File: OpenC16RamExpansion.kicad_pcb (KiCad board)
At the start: 2 copper layers, 51.1 x 45 mm, 6 parts, among them J1 C16-Exp-Port, U1 74LS257, U2 74LS257, U3 4464, U4 4464

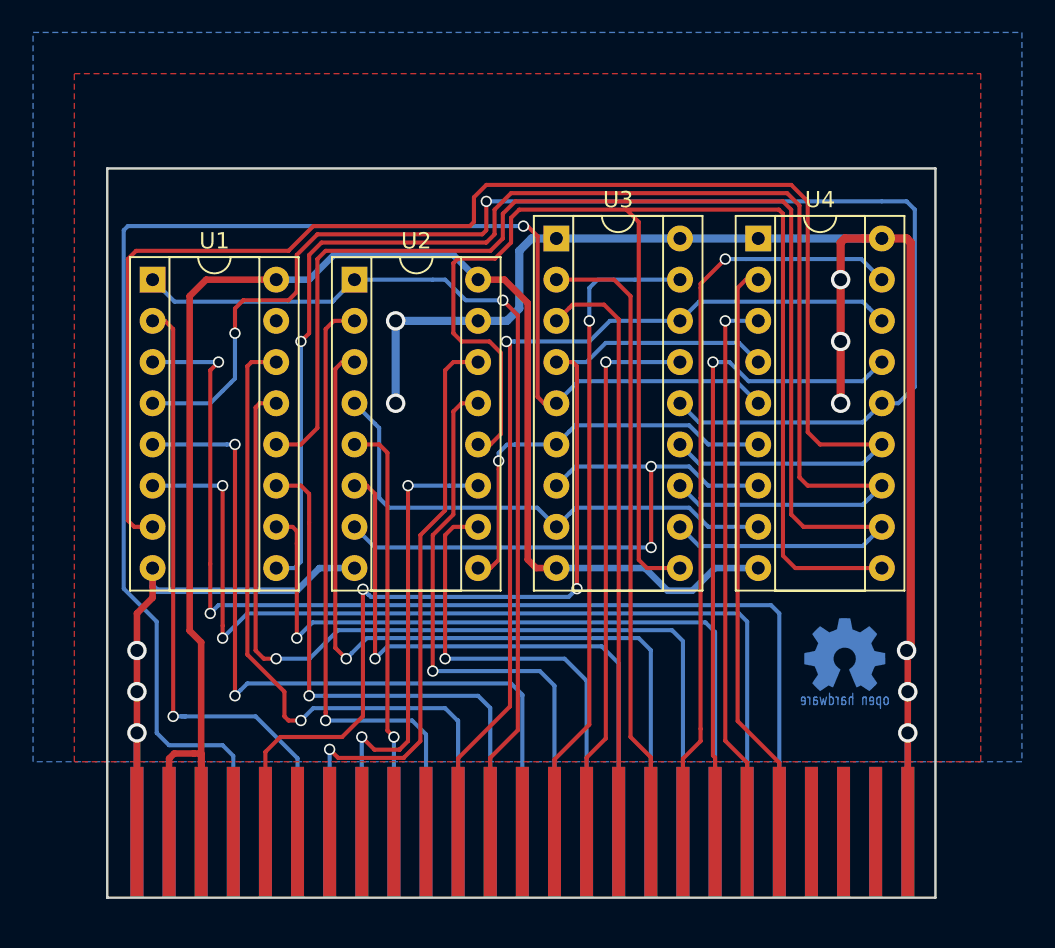
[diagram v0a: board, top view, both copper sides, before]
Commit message: Switch to new connector and improve back ground plane
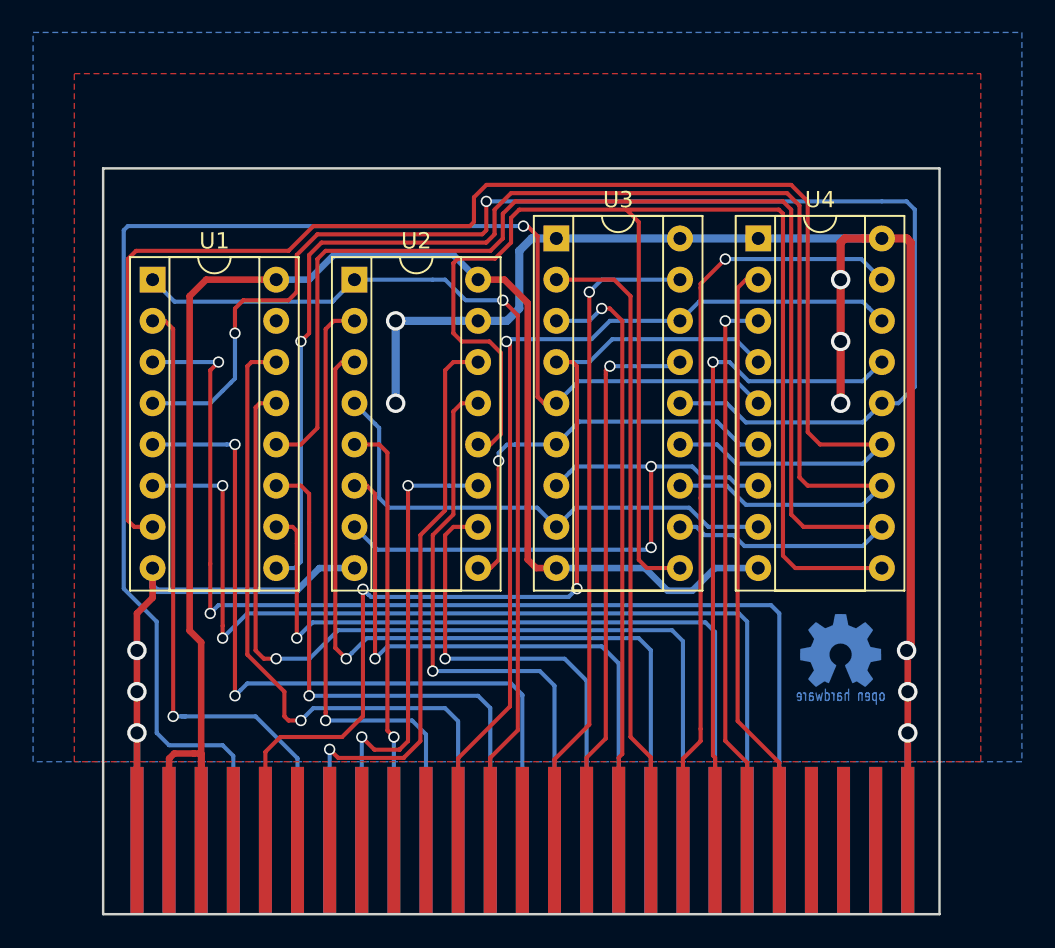
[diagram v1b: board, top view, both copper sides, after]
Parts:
- moved J1 1.00 mm to (149.5, 143.2)
- moved G*** 0.36 mm to (169.2, 127.0)
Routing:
- net /d5: track 36.2 -> 36.3 mm, vias 0 -> 1
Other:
- board size 51.1 x 45 mm -> 51.6 x 46 mm
- board text added: "V1.1"
- board text removed: "V1.0"

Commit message: Make connector lower again and smooth orners
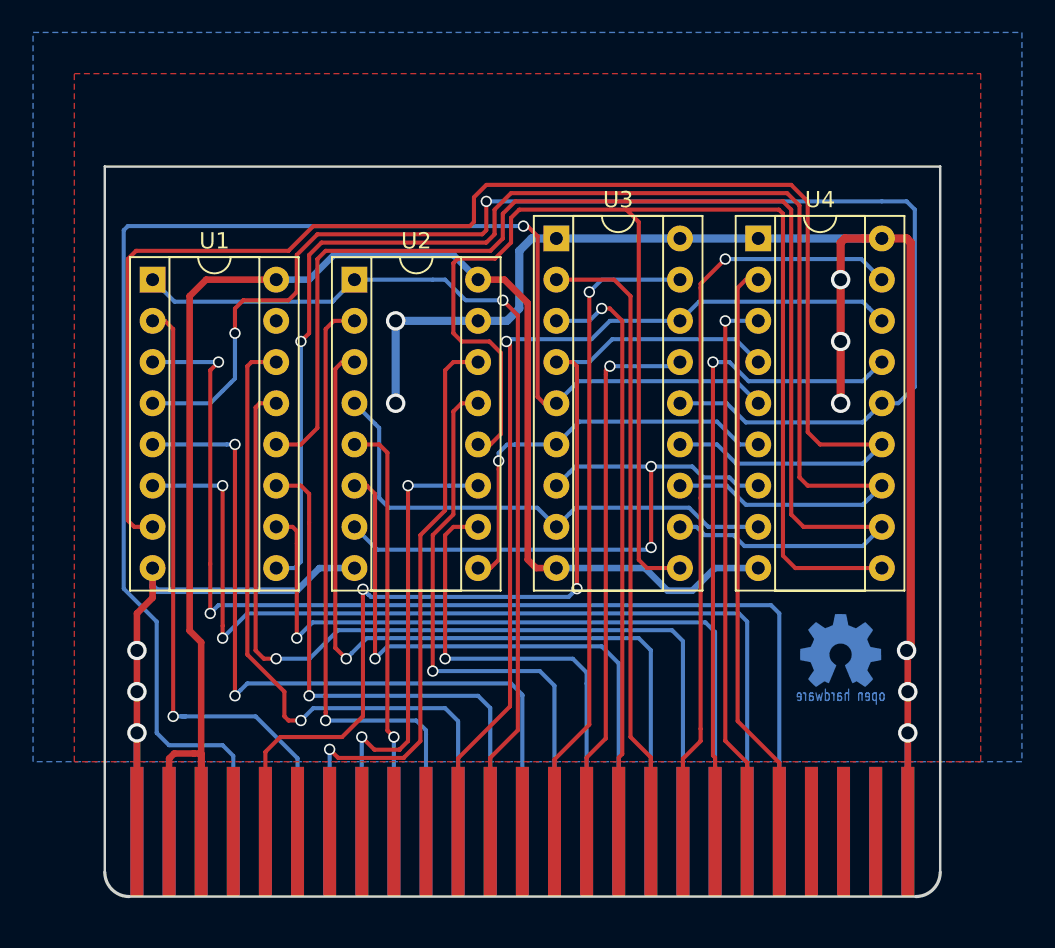
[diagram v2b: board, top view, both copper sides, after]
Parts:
- moved J1 5.00 mm to (149.5, 138.2)
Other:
- board size 51.6 x 46 mm -> 51.5 x 45 mm
- board text added: "github.com/SukkoPera/OpenC16RamExpansion"
- board text removed: "https://github.com/SukkoPera/OpenC16RamExpansion"

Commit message: Add decoupling caps
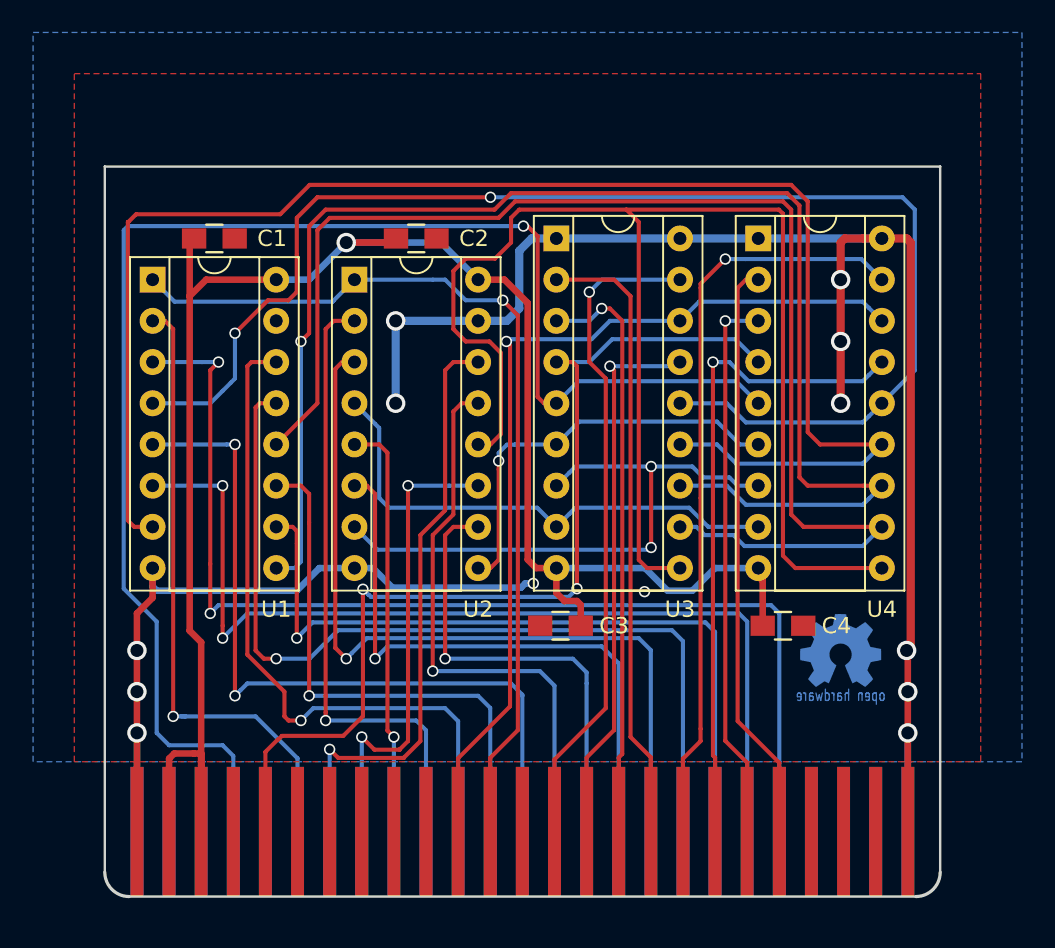
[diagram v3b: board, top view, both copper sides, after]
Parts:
- added C1: C, Capacitors_SMD:C_0805_HandSoldering, F.Cu at (130.6, 101.6)
- added C2: C, Capacitors_SMD:C_0805_HandSoldering, F.Cu at (143.0, 101.6)
- added C3: C, Capacitors_SMD:C_0805_HandSoldering, F.Cu at (151.9, 125.5)
- added C4: C, Capacitors_SMD:C_0805_HandSoldering, F.Cu at (165.6, 125.5)
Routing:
- net VCC: track 95.2 -> 112.1 mm, vias 0 -> 1
- net GND: track 133.5 -> 145.1 mm, vias 11 -> 12
- net /a0: track 84.1 -> 83.1 mm
- net /d7: track 40.1 -> 40.9 mm
- net /a3: track 83.3 -> 82.5 mm
- net (no net): vias 0 -> 1

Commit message: Space edge connector pins 2.0mm apart, improve ground plane and some other tweaks
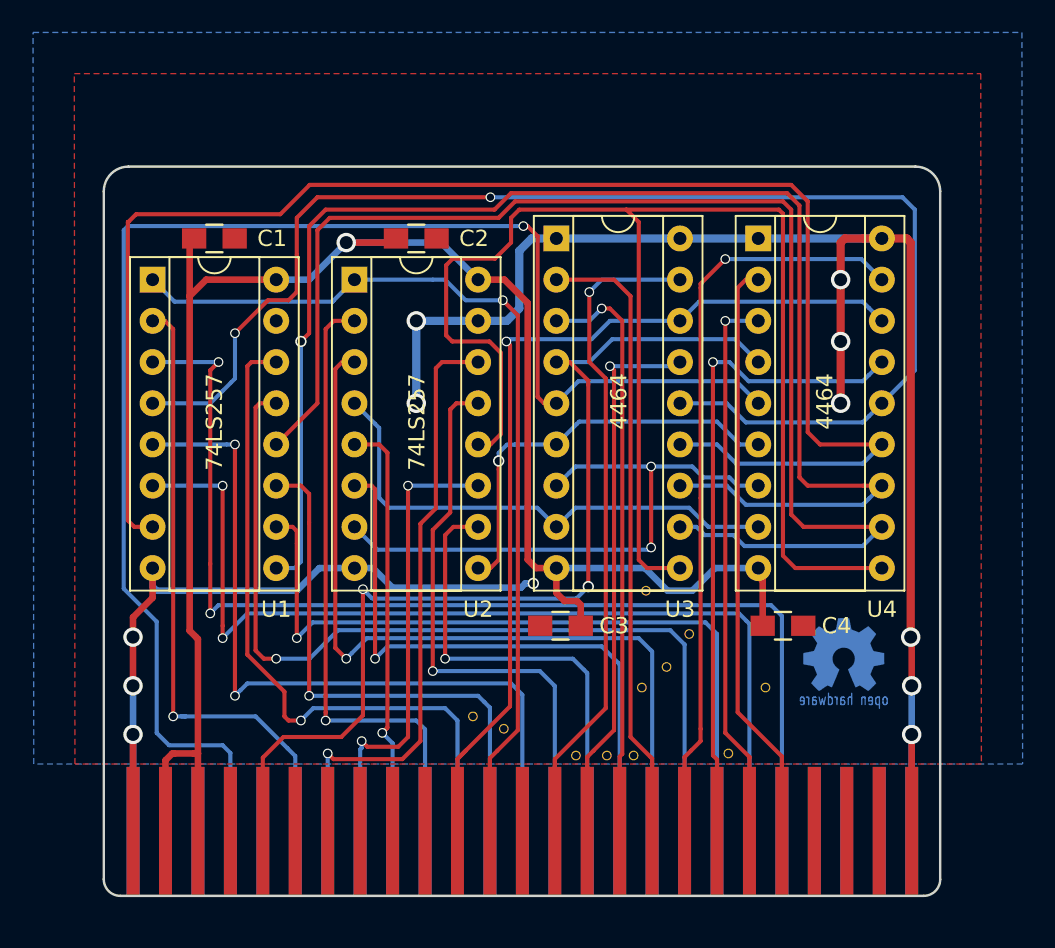
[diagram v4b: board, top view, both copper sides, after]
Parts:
- added REF**: VIA-0.6mm, OpenC16RamExpansion:VIA-0.6mm, F.Cu at (146.5, 131.1)
- added REF**: VIA-0.6mm, OpenC16RamExpansion:VIA-0.6mm, F.Cu at (156.4, 133.5)
- added REF**: VIA-0.6mm, OpenC16RamExpansion:VIA-0.6mm, F.Cu at (157.2, 123.3)
- added REF**: VIA-0.6mm, OpenC16RamExpansion:VIA-0.6mm, F.Cu at (148.4, 131.8)
- added REF**: VIA-0.6mm, OpenC16RamExpansion:VIA-0.6mm, F.Cu at (152.8, 133.5)
- added REF**: VIA-0.6mm, OpenC16RamExpansion:VIA-0.6mm, F.Cu at (154.7, 133.5)
- added REF**: VIA-0.6mm, OpenC16RamExpansion:VIA-0.6mm, F.Cu at (156.9, 129.3)
- added REF**: VIA-0.6mm, OpenC16RamExpansion:VIA-0.6mm, F.Cu at (158.4, 128.0)
- added REF**: VIA-0.6mm, OpenC16RamExpansion:VIA-0.6mm, F.Cu at (159.8, 126.0)
- added REF**: VIA-0.6mm, OpenC16RamExpansion:VIA-0.6mm, F.Cu at (164.5, 129.3)
- added REF**: VIA-0.6mm, OpenC16RamExpansion:VIA-0.6mm, F.Cu at (162.2, 133.3)
- J1: footprint C16_Cart_Conn:C16_Cart_Conn -> OpenC16RamExpansion:C16_Cart_Conn
- moved G*** 0.32 mm to (169.4, 127.3)
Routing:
- net GND: track 145.1 -> 143.5 mm
- net /a7: track 88.8 -> 90.2 mm
- net /r/w: track 62.0 -> 62.9 mm
- net VCC: track 112.1 -> 111.3 mm
- net //cas: track 56.3 -> 57.0 mm
- net /c16_a13: track 29.3 -> 28.7 mm
- net /c16_a10: track 43.2 -> 42.7 mm
- net (no net): vias 1 -> 0
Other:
- board size 51.5 x 45 mm -> 51.6 x 45 mm
- net class Default: clearance 0.2032 -> 0.1524
- net class Power: via_dia 1.2 -> 0.8; via_drill 0.8 -> 0.7
- rule pad_to_mask_clearance: 0.2 -> 0
- rule trace_clearance: 0.2032 -> 0.1524
- board text added: "V2"
- board text removed: "V1.1"

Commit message: Make board slightly larger
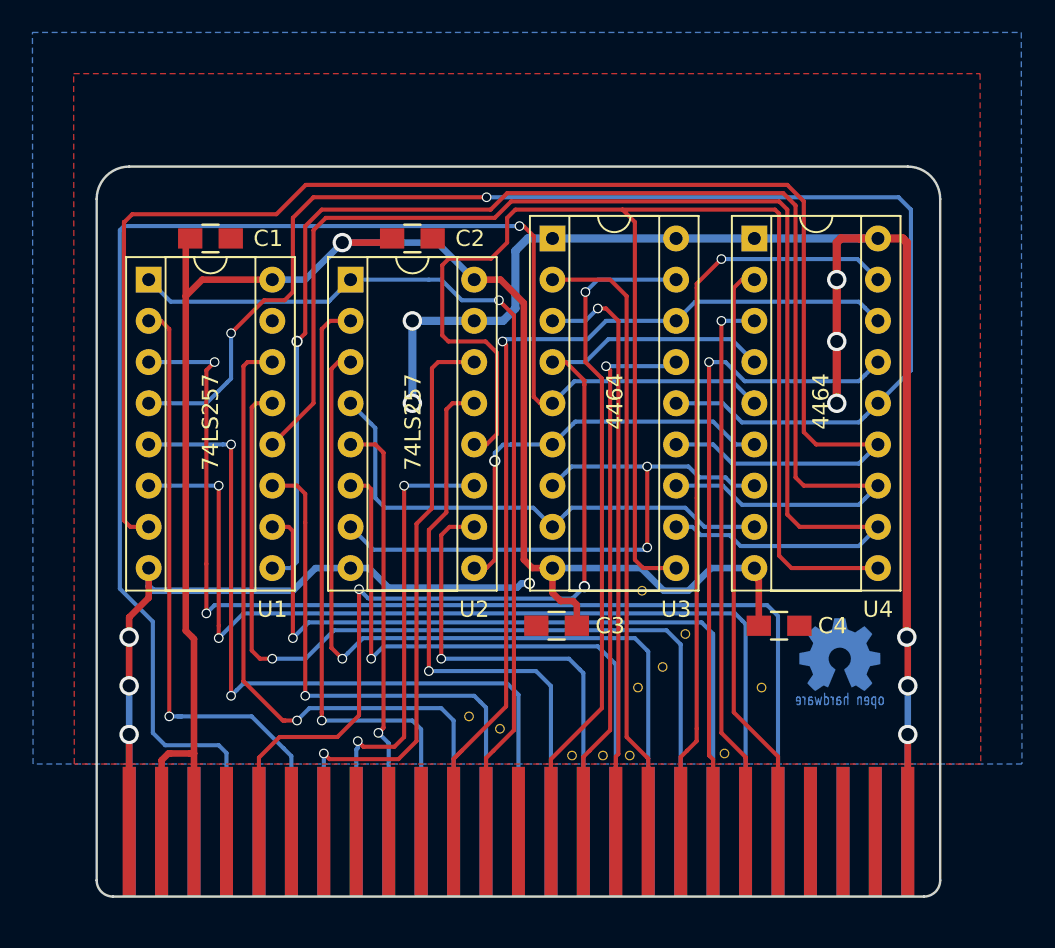
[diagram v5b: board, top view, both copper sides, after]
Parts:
- moved C1 0.24 mm to (130.3, 101.6)
- moved C2 0.24 mm to (142.8, 101.6)
- moved C3 0.24 mm to (151.7, 125.5)
- moved C4 0.24 mm to (165.4, 125.5)
- moved G*** 0.24 mm to (169.1, 127.3)
- moved J1 0.24 mm to (149.3, 138.2)
- moved REF** 0.24 mm to (146.3, 131.1)
- moved REF** 0.24 mm to (156.2, 133.5)
- moved REF** 0.24 mm to (156.9, 123.3)
- moved REF** 0.24 mm to (148.2, 131.8)
- moved REF** 0.24 mm to (154.5, 133.5)
- moved REF** 0.24 mm to (159.6, 126.0)
- moved U2 0.24 mm to (139.0, 104.1)
- moved U3 0.24 mm to (151.4, 101.6)
- moved U4 0.24 mm to (163.8, 101.6)
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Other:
- board size 51.6 x 45 mm -> 52 x 45 mm
